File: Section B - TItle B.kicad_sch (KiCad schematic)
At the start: 2 parts

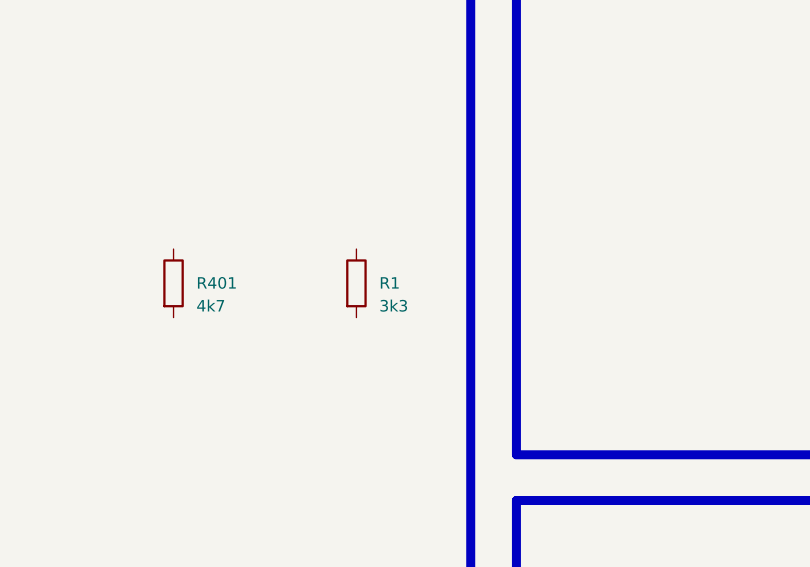
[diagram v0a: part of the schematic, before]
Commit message: dev: re-annotate duplicate R1 in Section B as R403
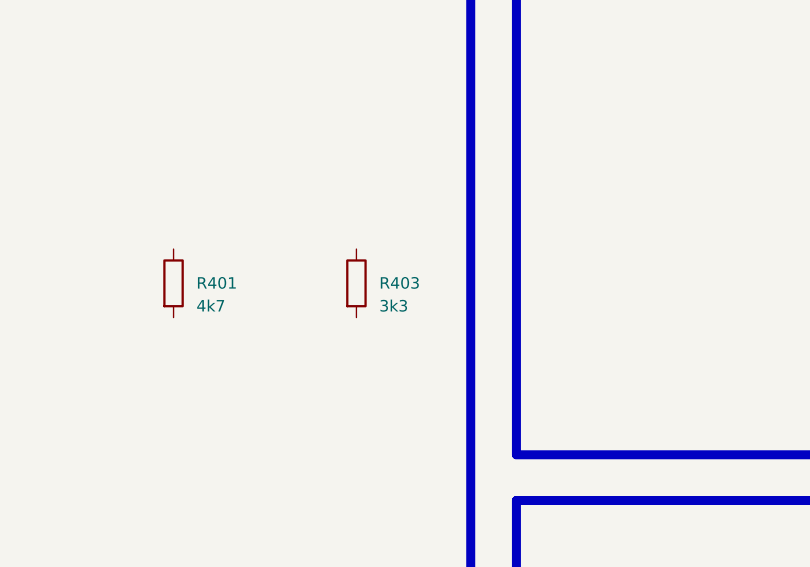
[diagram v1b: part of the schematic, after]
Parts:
- renumbered R1 to R403
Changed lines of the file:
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@@
 		(on_board yes)
 		(dnp no)
-		(property "Reference" "R1"
+		(property "Reference" "R403"
 			(at 124.46000000000001 101.6 0)
 			(effects (font (size 1.27 1.27)) (justify left))
@@
 			(project "ci_dummy"
 				(path "/f9e05184-c88b-4a88-ae9c-ab2bdb32be7c/c5103ceb-5325-4a84-a025-9638a412984e/e744f3ce-03a6-44a6-8792-1447ef232b9a"
-					(reference "R1")
+					(reference "R403")
 					(unit 1)
 				)

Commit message: section-a: grant myself all sheets, edit B
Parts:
- added R404: 1k, Resistor_SMD:R_0603_1608Metric, symbol Device:R
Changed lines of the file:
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@@
+		)
+	)
+	(symbol
+		(lib_id "Device:R")
+		(at 142.24 101.6 0)
+		(unit 1)
+		(exclude_from_sim no)
+		(in_bom yes)
+		(on_board yes)
+		(dnp no)
+		(property "Reference" "R404"
+			(at 144.78 101.6 0)
+			(effects (font (size 1.27 1.27)) (justify left))
+		)
+		(property "Value" "1k"
+			(at 144.78 104.14 0)
+			(effects (font (size 1.27 1.27)) (justify left))
+		)
+		(property "Footprint" "Resistor_SMD:R_0603_1608Metric"
+			(at 142.24 101.6 0)
+			(effects (font (size 1.27 1.27)) (hide yes))
+		)
+		(property "Datasheet" "~"
+			(at 142.24 101.6 0)
+			(effects (font (size 1.27 1.27)) (hide yes))
+		)
+		(pin "1")
+		(pin "2")
+		(instances
+			(project "ci_dummy"
+				(path "/f9e05184-c88b-4a88-ae9c-ab2bdb32be7c/c5103ceb-5325-4a84-a025-9638a412984e/e744f3ce-03a6-44a6-8792-1447ef232b9a"
+					(reference "R404")
+					(unit 1)
+				)
+			)
 		)
 	)

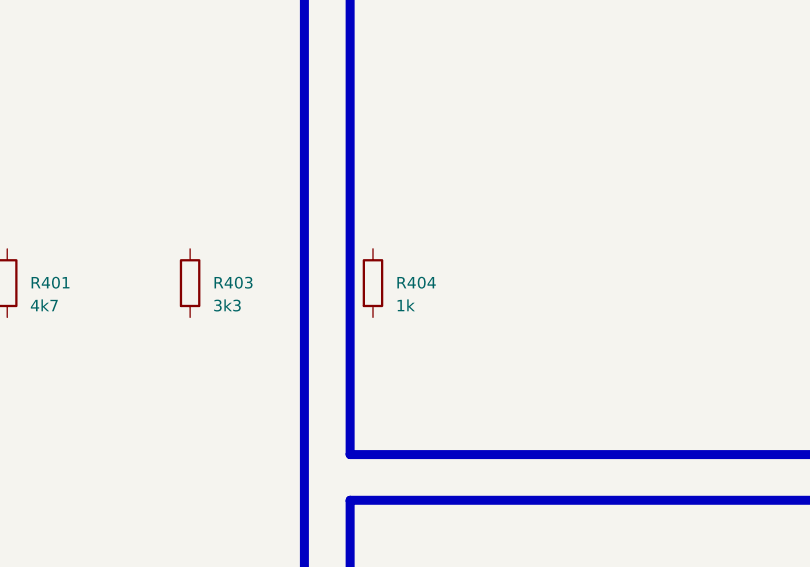
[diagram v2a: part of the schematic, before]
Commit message: Revert "section-a: grant myself all sheets, edit B"
This reverts commit 251938f37402ec01835c63d89290224a217dfbed.
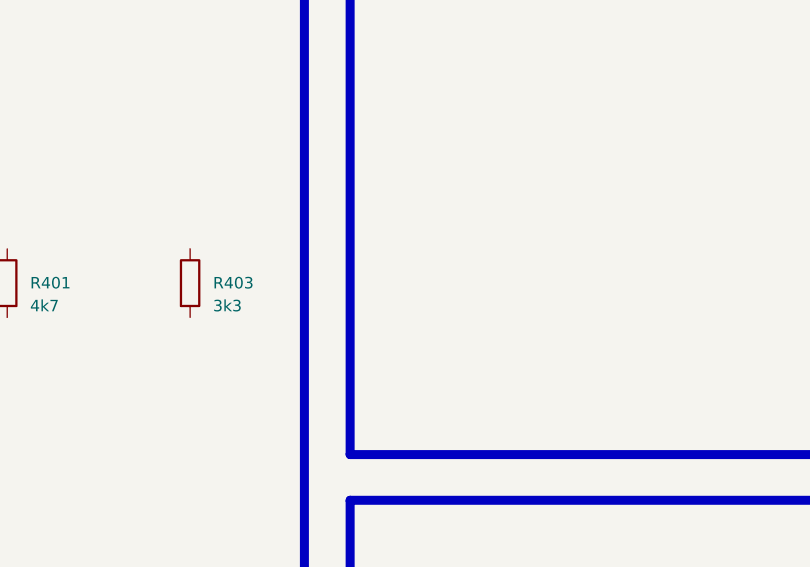
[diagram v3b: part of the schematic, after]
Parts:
- removed R404: 1k, Resistor_SMD:R_0603_1608Metric, symbol Device:R
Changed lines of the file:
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@@
-		)
-	)
-	(symbol
-		(lib_id "Device:R")
-		(at 142.24 101.6 0)
-		(unit 1)
-		(exclude_from_sim no)
-		(in_bom yes)
-		(on_board yes)
-		(dnp no)
-		(property "Reference" "R404"
-			(at 144.78 101.6 0)
-			(effects (font (size 1.27 1.27)) (justify left))
-		)
-		(property "Value" "1k"
-			(at 144.78 104.14 0)
-			(effects (font (size 1.27 1.27)) (justify left))
-		)
-		(property "Footprint" "Resistor_SMD:R_0603_1608Metric"
-			(at 142.24 101.6 0)
-			(effects (font (size 1.27 1.27)) (hide yes))
-		)
-		(property "Datasheet" "~"
-			(at 142.24 101.6 0)
-			(effects (font (size 1.27 1.27)) (hide yes))
-		)
-		(pin "1")
-		(pin "2")
-		(instances
-			(project "ci_dummy"
-				(path "/f9e05184-c88b-4a88-ae9c-ab2bdb32be7c/c5103ceb-5325-4a84-a025-9638a412984e/e744f3ce-03a6-44a6-8792-1447ef232b9a"
-					(reference "R404")
-					(unit 1)
-				)
-			)
 		)
 	)
